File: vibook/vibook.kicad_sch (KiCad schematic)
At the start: 53 parts, among them IC3 STLQ020C33R, J1 Conn_ARM_JTAG_SWD_10, SW3 SW_Push, U2 STM32L011K4Ux, U3 MPR121QR2, U5 MPR121QR2

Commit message: updated board design
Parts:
- removed U1, U4: ~, jlc:12matrix, symbol Terminals:12pin
- removed U6: ~, jlc:2pin, symbol Terminals:2pin
- added C12: 470u, Capacitor_Tantalum_SMD:CP_EIA-7360-38_Kemet-E, symbol Device:C
- added J2, J3: 6861XX148922_686112148922, 6861XX148922_686112148922:686112148922, symbol 6861XX148922_686112148922:6861XX148922_686112148922
- added U6: DFR0299, DFR0299:MODULE_DFR0299, symbol DFR0299:DFR0299
- U7: value ~ -> (none); footprint jlc:2pin -> Connector_Molex:Molex_PicoBlade_53047-0210_1x02_P1.25mm_Vertical
- U9: value ~ -> (none); footprint jlc:2pin -> Connector_PinHeader_2.54mm:PinHeader_1x02_P2.54mm_Horizontal
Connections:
- net GND: now also C12.1, J2.Z1, J2.Z2, J3.Z1, J3.Z2, U6.10 (GND), U6.7 (GND); no longer U7.2 (P2)
- net +4.5V: now reaches C6.2, IC3.1 (VIN), IC3.3 (EN), U9.1 (P1)
- net +4.5V: now also C12.2, U6.1 (VCC); no longer U7.1 (P1)
- net at R23.2: now also J3.5
- net at R27.2: now also J3.9
- net at R22.2: now also J3.4
- net at R25.2: now also J3.7
- net at R12.2: now also J2.6
- net at R18.2: now also J2.12
- net at R21.2: now also J3.3
- net at R11.2: now also J2.5
- net at R9.2: now also J2.3
- net at R14.2: now also J2.8
- net at R31.1: now also U6.3 (TX)
- net at R17.2: now also J2.11
- net at R19.2: now also J3.1
- net at R24.2: now also J3.6
- net at R16.2: now also J2.10
- net at R8.2: now also J2.2
- net at R7.2: now also J2.1
- net at R15.2: now also J2.9
- net at R13.2: now also J2.7
- net at R10.2: now also J2.4
- net at U2.9 (PA3): now also U6.2 (RX)
- net at R30.2: now also J3.12
- net at R20.2: now also J3.2
- net at R29.2: now also J3.11
- net at R28.2: now also J3.10
- net at R26.2: now also J3.8
- new net: U6.6 (SPK1), U7.1 (P1)
- new net: U6.8 (SPK2), U7.2 (P2)
- no-connect marks 22 -> 31
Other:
- moved on the sheet: R19, R20, R21, R22, R23, R24, R25, R26, R27, R28, R29, R30

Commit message: updated schematic
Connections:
- net +3.3V: now also R4.2, R5.2; no longer R4.1, R5.1
- net ELE1_4: now reaches J3.5, R23.2
- net ELE1_8: now reaches J3.9, R27.2
- net EXTI5: now reaches R6.2, U2.11 (PA5), U3.1 (~{IRQ})
- net EXTI5: no longer U5.1 (~{IRQ})
- net I2C1_SCL: now reaches U2.10 (PA4), U3.2 (SCL), U5.2 (SCL)
- net I2C1_SCL: now also R5.1; no longer R5.2
- net I2C1_SDA: now reaches U2.20 (PA10), U3.3 (SDA), U5.3 (SDA), U5.4 (ADDR)
- net I2C1_SDA: now also R4.1; no longer R4.2
- net ELE1_3: now reaches J3.4, R22.2
- net ELE1_6: now reaches J3.7, R25.2
- net ELE0_5: now reaches J2.6, R12.2
- net NRST: now reaches C5.1, J1.10 (~{RESET}), SW3.1, U2.4 (NRST)
- net ELE0_11: now reaches J2.12, R18.2
- net ELE1_2: now reaches J3.3, R21.2
- net ELE0_4: now reaches J2.5, R11.2
- net ELE0_2: now reaches J2.3, R9.2
- net ELE0_7: now reaches J2.8, R14.2
- net at U6.2 (RX): now also R31.2; no longer U2.9 (PA3)
- net USART2_RX: now reaches U6.3 (TX)
- net USART2_RX: now also U2.9 (PA3); no longer R31.1
- net USART2_TX: now reaches U2.8 (PA2)
- net USART2_TX: now also R31.1; no longer R31.2
- net ELE0_10: now reaches J2.11, R17.2
- net ELE1_0: now reaches J3.1, R19.2
- net ELE1_5: now reaches J3.6, R24.2
- net ELE0_9: now reaches J2.10, R16.2
- net EXTI6: now reaches U2.12 (PA6)
- net EXTI6: now also U5.1 (~{IRQ})
- net SYS_SWDIO: now reaches J1.2 (SWDIO/TMS), U2.23 (PA13)
- net SYS_SWCLK: now reaches J1.4 (SWCLK/TCK), U2.24 (PA14)
- net ELE0_0: now reaches J2.1, R7.2
- net ELE1_9: now reaches J3.10, R28.2
- net ELE1_10: now reaches J3.11, R29.2
- net ELE1_11: now reaches J3.12, R30.2
- net ELE1_1: now reaches J3.2, R20.2
- net ELE1_7: now reaches J3.8, R26.2
- net ELE0_6: now reaches J2.7, R13.2
- net ELE0_3: now reaches J2.4, R10.2
- net ELE0_1: now reaches J2.2, R8.2
- net ELE0_8: now reaches J2.9, R15.2
- no-connect marks 31 -> 30
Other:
- moved on the sheet: C1, C10, C11, C12, C2, C3, C4, C5, C6, C7, C8, C9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

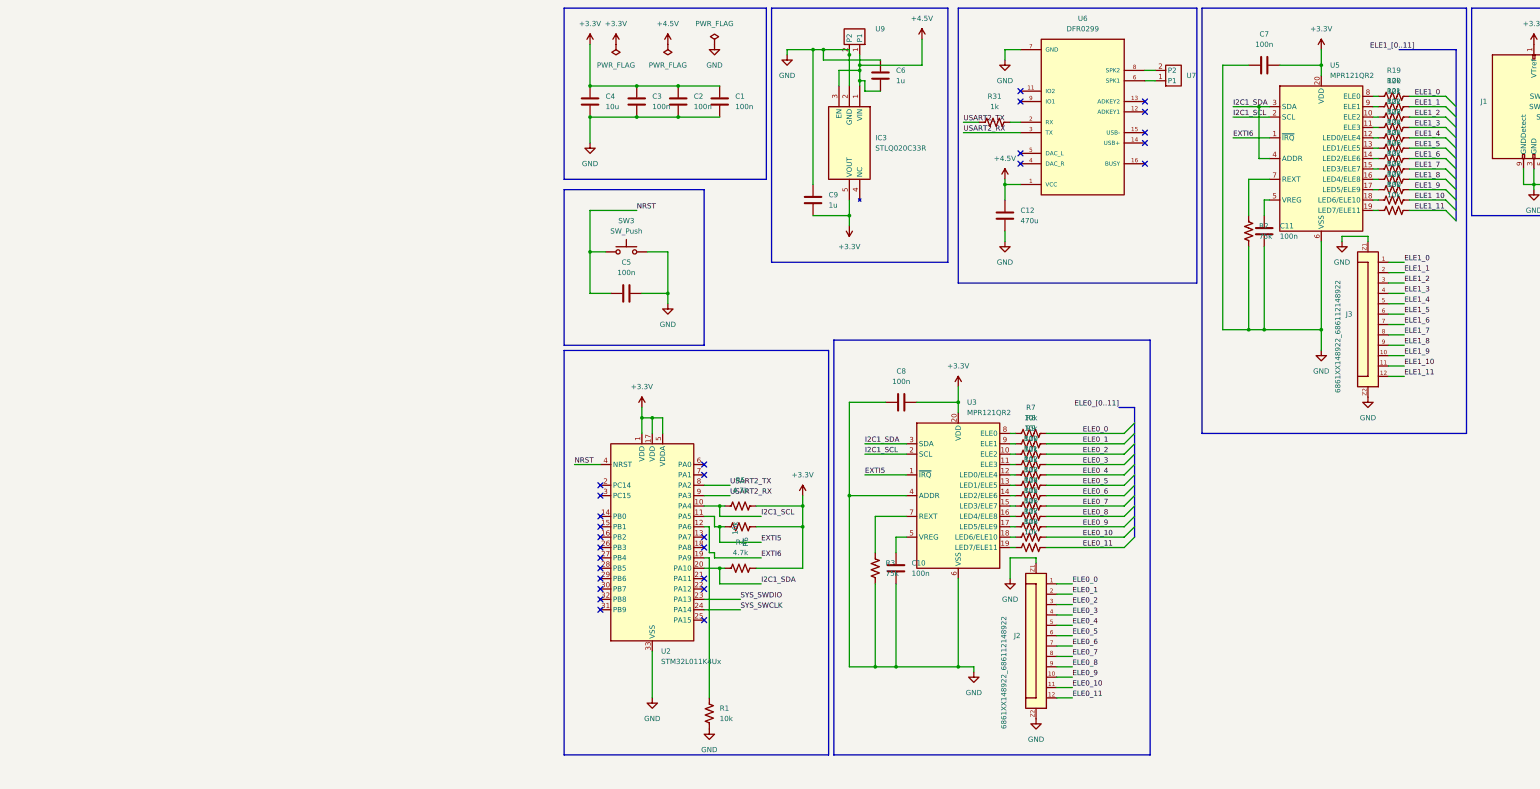
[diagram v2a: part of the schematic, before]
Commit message: changed ffc connectors and added different mcu
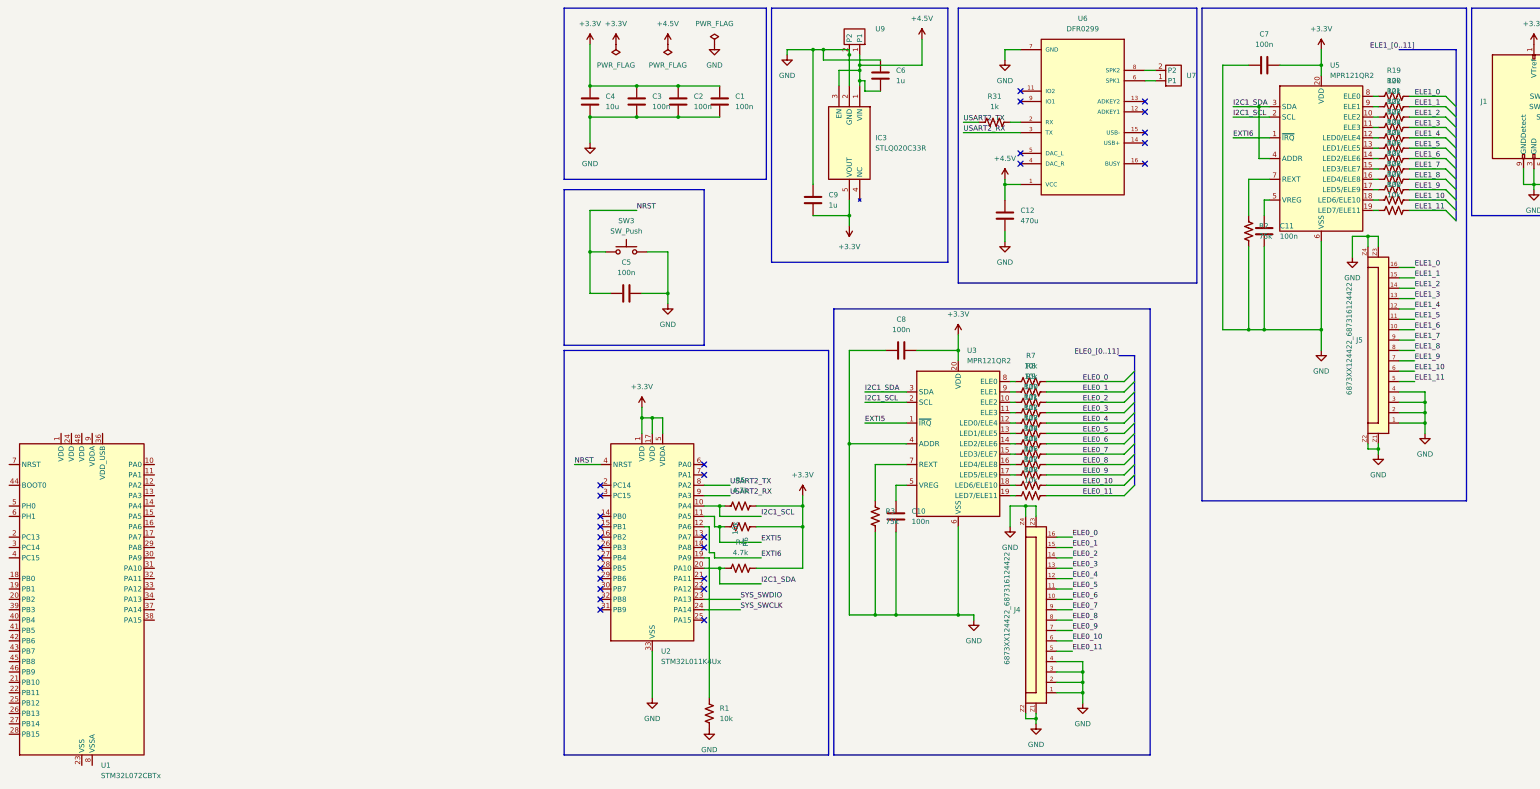
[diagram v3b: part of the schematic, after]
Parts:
- removed J2, J3: 6861XX148922_686112148922, 6861XX148922_686112148922:686112148922, symbol 6861XX148922_686112148922:6861XX148922_686112148922
- added J4, J5: 6873XX124422_687316124422, 687316124422:687316124422, symbol 6873XX124422_687316124422:6873XX124422_687316124422
- added U1: STM32L072CBTx, Package_QFP:LQFP-48_7x7mm_P0.5mm, symbol MCU_ST_STM32L0:STM32L072CBTx
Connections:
- net ELE0_0: now also J4.16
- net ELE0_1: now also J4.15
- net ELE0_10: now also J4.6
- net ELE0_11: now also J4.5
- net ELE0_2: now also J4.14
- net ELE0_3: now also J4.13
- net ELE0_4: now also J4.12
- net ELE0_5: now also J4.11
- net ELE0_6: now also J4.10
- net ELE0_7: now also J4.9
- net ELE0_8: now also J4.8
- net ELE0_9: now also J4.7
- net ELE1_0: now also J5.16
- net ELE1_1: now also J5.15
- net ELE1_10: now also J5.6
- net ELE1_11: now also J5.5
- net ELE1_2: now also J5.14
- net ELE1_3: now also J5.13
- net ELE1_4: now also J5.12
- net ELE1_5: now also J5.11
- net ELE1_6: now also J5.10
- net ELE1_7: now also J5.9
- net ELE1_8: now also J5.8
- net ELE1_9: now also J5.7
- net GND: now also J4.1, J4.2, J4.3, J4.4, J4.Z1, J4.Z2, J4.Z3, J4.Z4, J5.1, J5.2, J5.3, J5.4, J5.Z1, J5.Z2, J5.Z3, J5.Z4
- new net: U1.23 (VSS), U1.35 (VSS), U1.47 (VSS)
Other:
- moved on the sheet: C10, C8, R10, R11, R12, R13, R14, R15, R16, R17, R18, R3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

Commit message: started mcu upgrade and rerouting
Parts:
- removed SW3: SW_Push, Button_Switch_THT:SW_PUSH_6mm_H4.3mm, symbol Switch:SW_Push
- removed U2: STM32L011K4Ux, Package_DFN_QFN:QFN-32-1EP_5x5mm_P0.5mm_EP3.45x3.45mm, symbol MCU_ST_STM32L0:STM32L011K4Ux
- added C13, C14: 1u, Capacitor_SMD:C_0402_1005Metric, symbol Device:C
- added J6: 6873XX124422_687316124422, 687316124422:687316124422, symbol 6873XX124422_687316124422:6873XX124422_687316124422
- added R32, R33, R34, R35, R36, R37, R38, R39, R40, R41, R42, R43, R44, R45, R46, R47, R48: 10k, Resistor_SMD:R_0402_1005Metric, symbol Device:R_US
- added SW1: SKRPADE010, SKRPADE010_AAL, symbol 2026-04-09_20-31-23:SKRPADE010
- added U2: STM32U073RCTx, Package_QFP:LQFP-64_10x10mm_P0.5mm, symbol MCU_ST_STM32U0:STM32U073RCTx
- C1, C2, C3, C7, C8: value 100n -> 1u; footprint Capacitor_SMD:C_0805_2012Metric -> Capacitor_SMD:C_0402_1005Metric
- C10, C11, C5: footprint Capacitor_SMD:C_0805_2012Metric -> Capacitor_SMD:C_0402_1005Metric
- R1, R6: value 10k -> 4.7k; footprint Resistor_SMD:R_0603_1608Metric -> (none)
- R10, R11, R12, R13, R14, R15, R16, R17, R18, R19, R20, R21, R22, R23, R24, R25, R26, R27, R28, R29, R30, R7, R8, R9: footprint Resistor_SMD:R_0603_1608Metric -> Resistor_SMD:R_0402_1005Metric
- R4, R5: footprint Resistor_SMD:R_0603_1608Metric -> (none)
- U9: footprint Connector_PinHeader_2.54mm:PinHeader_1x02_P2.54mm_Horizontal -> Connector_Molex:Molex_PicoBlade_53047-0210_1x02_P1.25mm_Vertical
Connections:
- net EXTI6 is gone; now on net EXTI12: U5.1 (~{IRQ})
- net USART2_RX is gone; now on net USART4_RX: U6.3 (TX)
- net USART2_TX is gone; now on net USART4_TX: R31.1
- net +3.3V: now also R1.1, R4.1, R5.1, U1.1 (VDD), U1.24 (VDD), U1.36 (VDD_USB), U1.48 (VDD), U1.9 (VDDA), C13.1, C14.1; no longer R4.2, R5.2
- net ELE0_0: now also J4.6; no longer J4.16
- net ELE0_1: now also J4.8; no longer J4.15
- net ELE0_10: now also J4.7; no longer J4.6
- net ELE0_2: now also J4.10; no longer J4.14
- net ELE0_3: now also J4.12; no longer J4.13
- net ELE0_4: now also J4.14; no longer J4.12
- net ELE0_5: now also J4.16; no longer J4.11
- net ELE0_6: now also J4.15; no longer J4.10
- net ELE0_7: now also J4.13; no longer J4.9
- net ELE0_8: now also J4.11; no longer J4.8
- net ELE0_9: now also J4.9; no longer J4.7
- net ELE1_0: now also J5.6; no longer J5.16
- net ELE1_1: now also J5.8; no longer J5.15
- net ELE1_10: now also J5.7; no longer J5.6
- net ELE1_2: now also J5.10; no longer J5.14
- net ELE1_3: now also J5.12; no longer J5.13
- net ELE1_4: now also J5.14; no longer J5.12
- net ELE1_5: now also J5.16; no longer J5.11
- net ELE1_6: now also J5.15; no longer J5.10
- net ELE1_7: now also J5.13; no longer J5.9
- net ELE1_8: now also J5.11; no longer J5.8
- net ELE1_9: now also J5.9; no longer J5.7
- net GND: now also U1.23 (VSS), U1.35 (VSS), U1.47 (VSS), U1.8 (VSSA), C13.2, C14.2, J6.Z1, J6.Z2, J6.Z3, J6.Z4, R32.2, SW1.1, SW1.2; no longer R1.2
- net I2C1_SCL: now also R6.2, U1.30 (PA9); no longer R5.1
- net I2C1_SDA: now also R5.2, U1.31 (PA10); no longer R4.1
- net NRST: now also U1.7 (NRST), SW1.3; no longer C5.1
- net SYS_SWCLK: now also U1.37 (PA14)
- net SYS_SWDIO: now also U1.34 (PA13)
- net USART4_TX: now reaches U1.10 (PA0)
- net USART4_RX: now reaches U1.11 (PA1)
- net TSC0: now reaches U1.12 (PA2)
- net TSC0: now also R47.2
- net TSC1: now reaches U1.13 (PA3)
- net TSC1: now also R45.2
- net TSC2: now reaches U1.15 (PA5)
- net TSC2: now also R43.2
- net TSC3: now reaches U1.16 (PA6)
- net TSC3: now also R41.2
- net TSC4: now reaches U1.17 (PA7)
- net TSC4: now also R39.2
- net TSC5: now reaches U1.18 (PB0)
- net TSC5: now also R37.2
- net TSC6: now reaches U1.19 (PB1)
- net TSC6: now also R35.2
- net TSC7: now reaches U1.20 (PB2)
- net TSC7: now also R33.2
- net TSC12: now reaches U1.22 (PB11)
- net TSC12: now also R34.2
- net TSC13: now reaches U1.25 (PB12)
- net TSC13: now also R36.2
- net TSC14: now reaches U1.26 (PB13)
- net TSC14: now also R38.2
- net TSC15: now reaches U1.27 (PB14)
- net TSC15: now also R40.2
- net EXTI11: now reaches U1.32 (PA11)
- net EXTI11: now also R4.2, U3.1 (~{IRQ})
- net EXTI12: now reaches U1.33 (PA12)
- net EXTI12: now also R1.2
- net TSC8: now reaches U1.39 (PB3)
- net TSC8: now also R42.2
- net TSC9: now reaches U1.40 (PB4)
- net TSC9: now also R44.2
- net TSC10: now reaches U1.42 (PB6)
- net TSC10: now also R46.2
- net TSC11: now reaches U1.43 (PB7)
- net TSC11: now also R48.2
- net at U1.44 (BOOT0): now also R32.1
- removed net EXTI5: R6.2, U3.1 (~{IRQ})
- new net: J6.10, R39.1
- new net: J6.6, R43.1
- new net: J6.5, R44.1
- new net: J6.14, R35.1
- new net: J6.4, R45.1
- new net: J6.15, R34.1
- new net: J6.13, R36.1
- new net: J6.12, R37.1
- new net: J6.7, R42.1
- new net: J6.9, R40.1
- new net: J6.1, R48.1
- new net: J6.11, R38.1
- new net: J6.16, R33.1
- new net: J6.2, R47.1
- new net: J6.3, R46.1
- new net: J6.8, R41.1
- new net: C5.1, SW1.4
- new net: U2.18 (VSS), U2.31 (VSS), U2.47 (VSS), U2.63 (VSS)
- no-connect marks 30 -> 24
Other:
- moved on the sheet: C10, C5, C8, J4, R10, R11, R12, R13, R14, R15, R16, R17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

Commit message: finished spine pcb final design, sent for manufacture
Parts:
- removed R1, R4, R5, R6: 4.7k, symbol Device:R_US
- removed U2: STM32U073RCTx, Package_QFP:LQFP-64_10x10mm_P0.5mm, symbol MCU_ST_STM32U0:STM32U073RCTx
- added C15, C16, C17, C18, C19, C20: 47n, Capacitor_SMD:C_0402_1005Metric, symbol Device:C
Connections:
- net EXTI11: now also U1.41 (PB5); no longer U1.32 (PA11)
- net EXTI12: now also U1.28 (PB15); no longer U1.33 (PA12)
- net GND: now also C15.2, C16.2, C17.2, C18.2, C19.2, C20.2
- net I2C1_SCL: now also U1.45 (PB8); no longer U1.30 (PA9)
- net I2C1_SDA: now also U1.46 (PB9); no longer U1.31 (PA10)
- net TSC_G2_1: now reaches U1.14 (PA4)
- net TSC_G2_1: now also C16.1
- net LPUART1_TX: now reaches U1.21 (PB10)
- net LPUART1_TX: now also R31.1
- net TSC0 renamed TSC_G1_2
- net TSC_G1_2: now also U1.11 (PA1); no longer U1.12 (PA2)
- net TSC1 renamed TSC_G1_3
- net TSC_G1_3: now also U1.12 (PA2); no longer U1.13 (PA3)
- net TSC10 renamed TSC_G5_1
- net TSC_G5_1: now also U1.39 (PB3); no longer U1.42 (PB6)
- net TSC11: no longer names the net of U1.43 (PB7)
- net TSC11: no longer R48.2
- net TSC12 renamed TSC_G6_1
- net TSC_G6_1: now also C20.1; no longer R34.2
- net TSC13 renamed TSC_G6_2
- net TSC_G6_2: now also R34.2; no longer R36.2
- net TSC14 renamed TSC_G6_3
- net TSC_G6_3: now also R36.2; no longer R38.2
- net TSC15 renamed TSC_G4_2
- net TSC_G4_2: now also U1.31 (PA10); no longer U1.27 (PB14)
- net TSC2 renamed TSC_G1_4
- net TSC_G1_4: now also U1.13 (PA3); no longer U1.15 (PA5)
- net TSC3 renamed TSC_G2_2
- net TSC_G2_2: now also U1.15 (PA5); no longer U1.16 (PA6)
- net TSC4 renamed TSC_G2_3
- net TSC_G2_3: now also U1.16 (PA6); no longer U1.17 (PA7)
- net TSC5 renamed TSC_G2_4
- net TSC_G2_4: now also U1.17 (PA7); no longer U1.18 (PB0)
- net TSC6 renamed TSC_G3_3
- net TSC7 renamed TSC_G3_4
- net TSC8 renamed TSC_G4_3
- net TSC_G4_3: now also U1.32 (PA11); no longer U1.39 (PB3)
- net TSC9 renamed TSC_G4_4
- net TSC_G4_4: now also U1.33 (PA12); no longer U1.40 (PB4)
- net USART4_RX: no longer names the net of U6.3 (TX)
- net USART4_RX: no longer U1.11 (PA1)
- net USART4_TX renamed TSC_G1_1
- net TSC_G1_1: now also C15.1; no longer R31.1
- new net TSC_G3_2: C17.1, U1.18 (PB0)
- new net TSC_G4_1: C18.1, U1.30 (PA9)
- new net TSC_G5_2: R48.2, U1.40 (PB4)
- new net TSC_G5_3: C19.1, U1.42 (PB6)
- new net TSC_G6_4: R38.2, U1.27 (PB14)
- no-connect marks 24 -> 20
